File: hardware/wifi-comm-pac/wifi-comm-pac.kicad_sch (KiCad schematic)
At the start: 71 parts, among them J1 Conn_02x05 IDC (P1 MODEM), J2 CMS-151103-088SP, J3 USB-C sink, SW1 Slide switch, latching, U1 74LVC4T245 (TXD/MCB), U10 AP2112K-3.3 LDO, U2 74LVC4T245 (CTS/RI), U3 74LVC1G07 (MSB), U4 MAX3232 (RXD), U5 ESP32-S2-MINI-2U, U6 AW9523B panel 0x58, U7 AW9523B interface 0x59, U8 MAX98357A, U9 TPS54331 buck 12.6->5

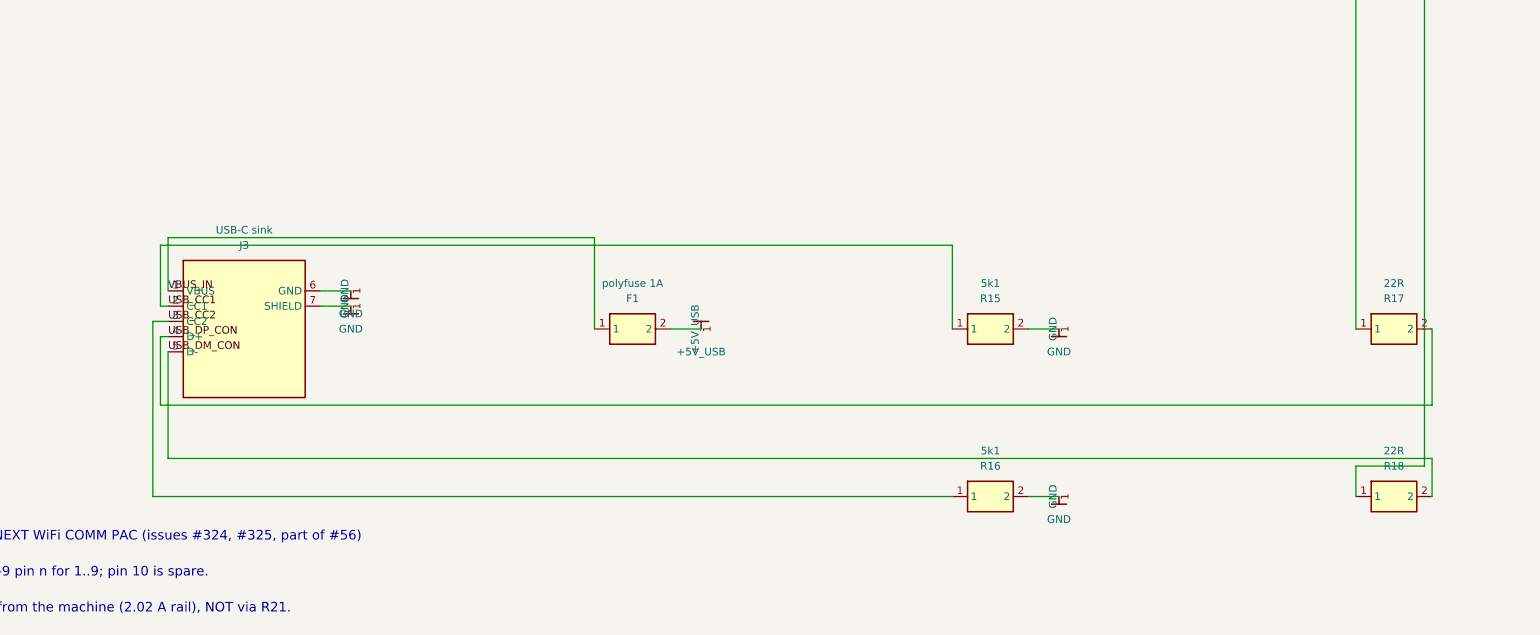
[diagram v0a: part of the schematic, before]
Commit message: hardware: rebuild J3 to all 30 USB-C pins and assign its footprint (#325)
J3 was the last open footprint, and it was blocked on its SYMBOL, not on a part
decision: the symbol had 7 pins against the footprint's 30 pads, so assigning it
would have left 23 pads with no net.

The pin map was not missing -- it was in the SnapEDA zip that supplied the
footprint, as UJ32-C-H-G-DSMT-1-P24-TR.kicad_sym. I had recorded it as "waiting
for the real pin map" while the map sat extracted on disk. It has now been read.

J3 is rebuilt with the part's own numbers, which makes it the one symbol on this
board that does not use logical pin numbers:

  A1 A12 B1 B12   GND        (all four ground returns)
  A4 A9 B4 B9     VBUS_IN    (whichever pair the cable presents)
  A5              USB_CC1    -> R15 5k1 to GND (the sink's Rd)
  B5              USB_CC2    -> R16 5k1 to GND
  A6 B6           USB_DP_CON -> R17 22R
  A7 B7           USB_DM_CON -> R18 22R
  SH1..SH6        GND        (the shell is the ground path)
  A2 A3 A10 A11   NC  \
  B2 B3 B10 B11   NC   > the 8 SuperSpeed contacts
  A8 B8           NC  /  and both SBU

The ten unused contacts are **carried and marked no-connect rather than
omitted**, so each gets a marker on its pad instead of being silently left
floating -- an omitted pin is a pad with no net, which is exactly how a USB-C
footprint ends up half-wired.

Both halves of the USB 2.0 pair are wired (A6/B6 and A7/B7). Wiring only one
half is the classic way to get a port that works with the cable one way up and
not the other, and the sheet looks fine either way -- so check_schematics.py now
asserts the exact node sets for VBUS_IN, USB_CC1/2 and USB_DP/DM_CON, and asserts
J3's ten unused pins are genuinely unconnected.

Two fixes in the checker, both of which would otherwise have gone quiet:

  - excludes_nets["+12V"] read pins("J3", range(1, 8)).  Against A1/B1-style
    numbers that matches NOTHING, so the assertion would have passed while
    asserting nothing.  Now p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
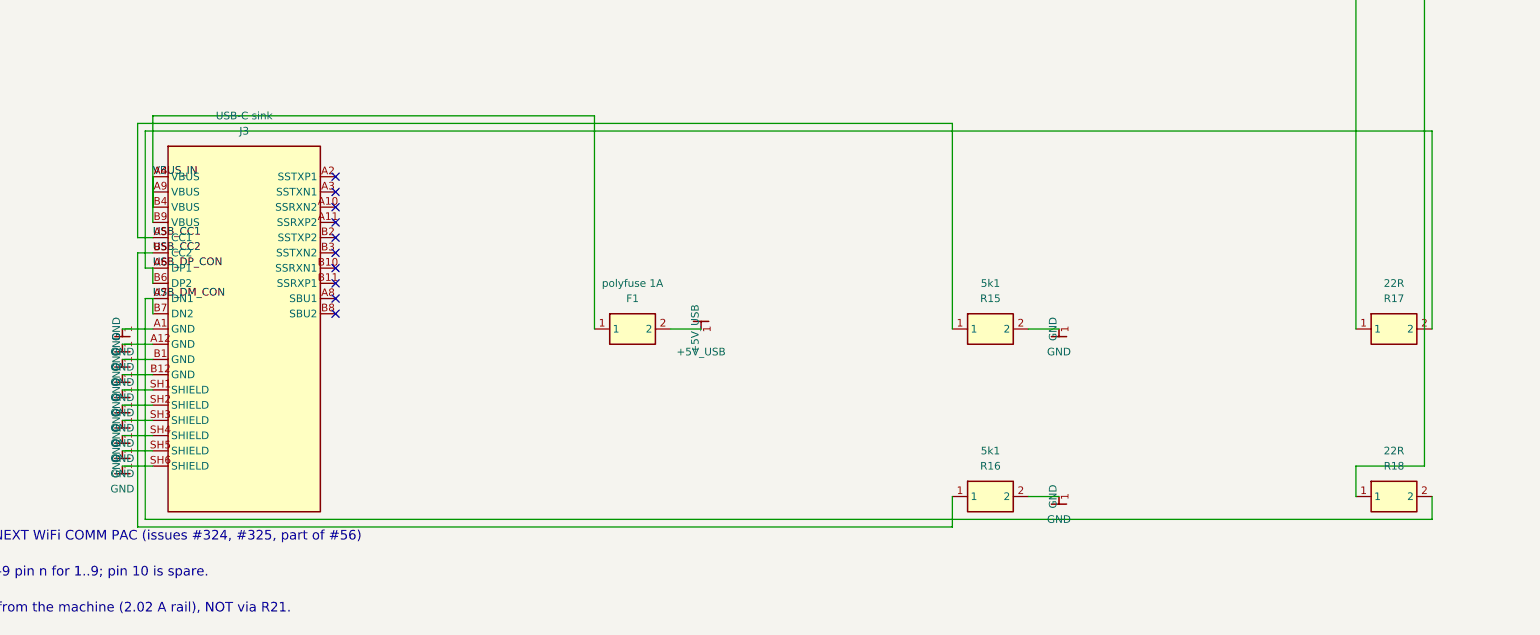
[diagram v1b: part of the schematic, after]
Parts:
- J3: footprint (none) -> o1next:USB_C_SameSky_UJ32-C-H-G-DSMT-1-P24-TR
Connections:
- net GND: now also J3.A1 (GND), J3.A12 (GND), J3.B1 (GND), J3.B12 (GND), J3.SH1 (SHIELD), J3.SH2 (SHIELD), J3.SH3 (SHIELD), J3.SH4 (SHIELD), J3.SH5 (SHIELD), J3.SH6 (SHIELD); no longer J3.6 (GND), J3.7 (SHIELD)
- net USB_CC1: now also J3.A5 (CC1); no longer J3.2 (CC1)
- net USB_CC2: now also J3.B5 (CC2); no longer J3.3 (CC2)
- net USB_DM_CON: now also J3.A7 (DN1), J3.B7 (DN2); no longer J3.5 (D-)
- net USB_DP_CON: now also J3.A6 (DP1), J3.B6 (DP2); no longer J3.4 (D+)
- net VBUS_IN: now also J3.A4 (VBUS), J3.A9 (VBUS), J3.B4 (VBUS), J3.B9 (VBUS); no longer J3.1 (VBUS)
- no-connect marks 27 -> 37
